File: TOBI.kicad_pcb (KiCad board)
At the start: 4 copper layers, 50.8 x 50.8 mm, 23 parts, among them J1 Battery Connector, J2 Top Screw Terminal, J3 Bottom Screw Terminal, Q1 Q_NMOS_GDS, Q2 Q_NMOS_GDS, Q3 Q_NMOS_GDS, U1 XIAO-ESP32-S3-SMD, U2 LSM6DSO32, U4 MS5611-01BA

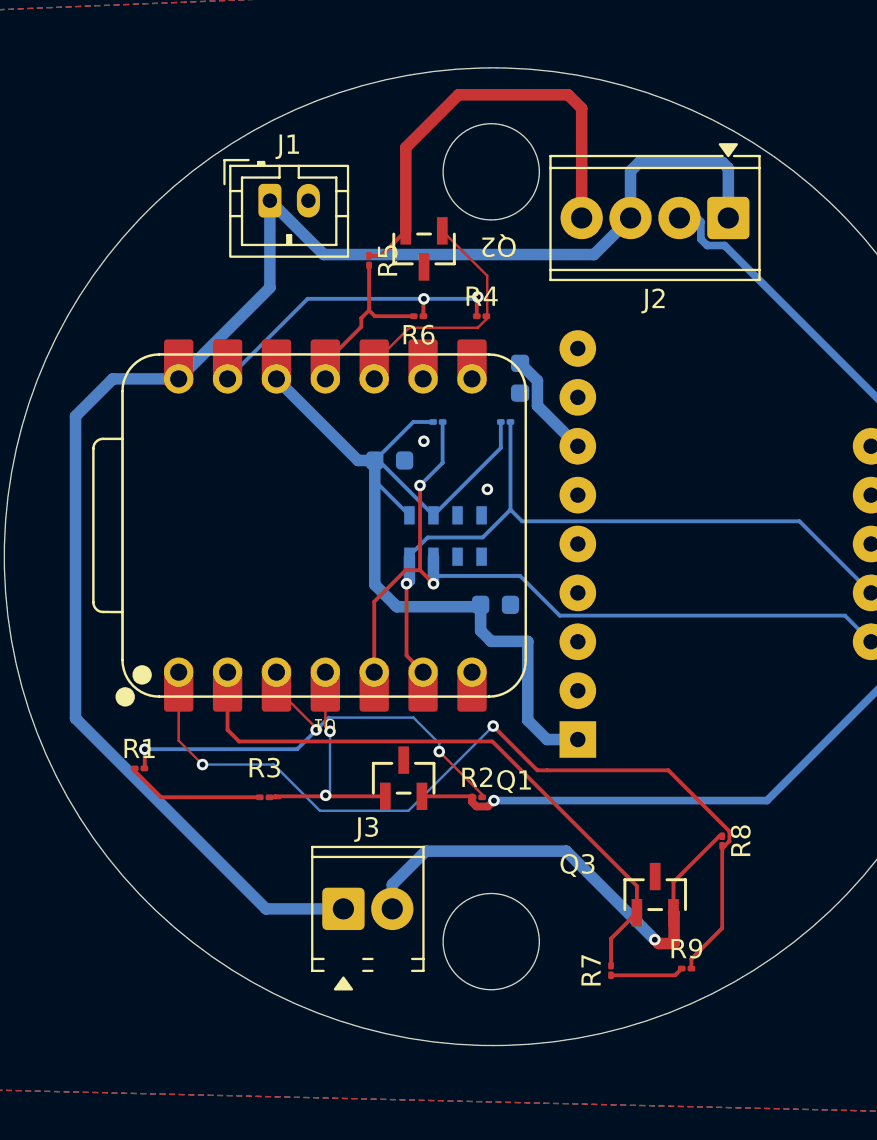
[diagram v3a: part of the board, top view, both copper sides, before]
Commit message: Silkscreen Text Modifications
Added more descriptive text, edited sizes for labeling, as well as general board info text.
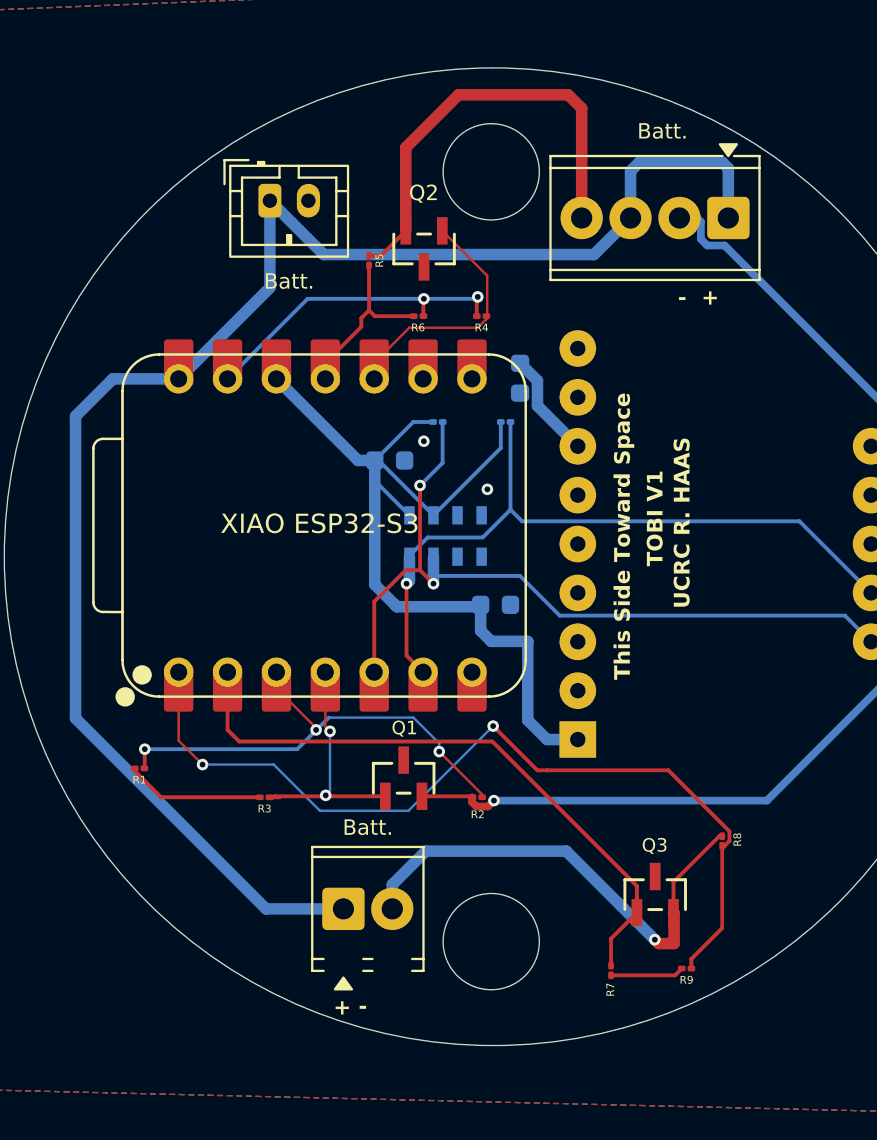
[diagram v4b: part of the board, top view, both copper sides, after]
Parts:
- XIAO ESP32-S3: renamed from U1
- renumbered J3 to Batt., J2 to Batt., J1 to Batt., U4 to IMU, U2 to LSM6DSO32
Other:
- board text added: "+ -"
- board text added: "- +"
- board text added: "TOBI V1"
- board text added: "This Side Toward Space"
- board text added: "UCRC R. HAAS"
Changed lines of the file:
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@@
 		(tags "resistor")
 		(property "Reference" "R5"
-			(at 0 -1 90)
+			(at 0 -0.549199 90)
 			(layer "F.SilkS")
 			(effects
 				(font
-					(size 1 1)
-					(thickness 0.15)
+					(size 0.4 0.4)
+					(thickness 0.05)
 				)
 			)
@@
 		(tags "T2N7002BK_LM ")
 		(property "Reference" "Q1"
-			(at 5.760001 0.1298 0)
+			(at 0.049999 -2.610201 0)
 			(unlocked yes)
 			(layer "F.SilkS")
 			(effects
 				(font
-					(size 1 1)
-					(thickness 0.15)
+					(size 0.7 0.7)
+					(thickness 0.0875)
 				)
 			)
@@
 		(tags "resistor")
 		(property "Reference" "R3"
-			(at 0 -1.5 0)
+			(at 0 0.6 0)
 			(layer "F.SilkS")
 			(effects
 				(font
-					(size 1 1)
-					(thickness 0.15)
+					(size 0.4 0.4)
+					(thickness 0.05)
 				)
 			)
@@
 		(layer "F.Cu")
 		(at 183.88 100.88 180)
-		(property "Reference" "U1"
-			(at 0.025 -10.35 180)
+		(property "Reference" "XIAO ESP32-S3"
+			(at 0.28 0.08 0)
 			(unlocked yes)
 			(layer "F.SilkS")
 			(effects
 				(font
-					(size 0.635 0.635)
-					(thickness 0.1016)
+					(size 1 1)
+					(thickness 0.125)
 				)
 			)
@@
 		(descr "Terminal Block Phoenix MPT-0,5-2-2.54, 2 pins, pitch 2.54mm, size 5.54x6.2mm, drill diameter 1.1mm, pad diameter 2.2mm, http://www.mouser.com/ds/2/324/ItemDetail_1725656-920552.pdf, script-generated using https://gitlab.com/kicad/libraries/kicad-footprint-generator/-/tree/master/scripts/TerminalBlock_Phoenix")
 		(tags "THT Terminal Block Phoenix MPT-0,5-2-2.54 pitch 2.54mm size 5.54x6.2mm drill 1.1mm pad 2.2mm")
-		(property "Reference" "J3"
+		(property "Reference" "Batt."
 			(at 1.27 -4.22 0)
 			(layer "F.SilkS")
 			(effects
 				(font
-					(size 1 1)
-					(thickness 0.15)
+					(size 0.8 0.8)
+					(thickness 0.1)
 				)
 			)
@@
 		(tags "resistor")
 		(property "Reference" "R1"
-			(at 0 -1 0)
+			(at 0 0.6 0)
 			(layer "F.SilkS")
 			(effects
 				(font
-					(size 1 1)
-					(thickness 0.15)
+					(size 0.4 0.4)
+					(thickness 0.05)
 				)
 			)
@@
 		(tags "resistor")
 		(property "Reference" "R9"
-			(at 0 -1 0)
+			(at 0 0.6 0)
 			(layer "F.SilkS")
 			(effects
 				(font
-					(size 1 1)
-					(thickness 0.15)
+					(size 0.4 0.4)
+					(thickness 0.05)
 				)
 			)
@@
 		(tags "resistor")
 		(property "Reference" "R2"
-			(at 0 -1 0)
+			(at 0.025 0.9 0)
 			(layer "F.SilkS")
 			(effects
 				(font
-					(size 1 1)
-					(thickness 0.15)
+					(size 0.4 0.4)
+					(thickness 0.05)
 				)
 			)
@@
 		(descr "Terminal Block Phoenix MPT-0,5-4-2.54, 4 pins, pitch 2.54mm, size 10.6x6.2mm, drill diameter 1.1mm, pad diameter 2.2mm, http://www.mouser.com/ds/2/324/ItemDetail_1725672-916605.pdf, script-generated using https://gitlab.com/kicad/libraries/kicad-footprint-generator/-/tree/master/scripts/TerminalBlock_Phoenix")
 		(tags "THT Terminal Block Phoenix MPT-0,5-4-2.54 pitch 2.54mm size 10.6x6.2mm drill 1.1mm pad 2.2mm")
-		(property "Reference" "J2"
-			(at 3.81 -4.22 0)
+		(property "Reference" "Batt."
+			(at 3.42 4.5 0)
 			(layer "F.SilkS")
 			(effects
 				(font
-					(size 1 1)
-					(thickness 0.15)
+					(size 0.8 0.8)
+					(thickness 0.1)
 				)
 			)
@@
 		(tags "T2N7002BK_LM ")
 		(property "Reference" "Q2"
-			(at -3.864999 0.1298 180)
+			(at 0.0108 2.908599 0)
 			(unlocked yes)
 			(layer "F.SilkS")
 			(effects
 				(font
-					(size 1 1)
-					(thickness 0.15)
+					(size 0.8 0.8)
+					(thickness 0.1)
 				)
 			)
@@
 		(tags "resistor")
 		(property "Reference" "R6"
-			(at 0 -1 0)
+			(at 0.025 -0.6 0)
 			(layer "F.SilkS")
 			(effects
 				(font
-					(size 1 1)
-					(thickness 0.15)
+					(size 0.4 0.4)
+					(thickness 0.05)
 				)
 			)
@@
 		(tags "T2N7002BK_LM ")
 		(property "Reference" "Q3"
-			(at -4.019999 -1.5602 0)
+			(at -0.019999 -2.5602 0)
 			(unlocked yes)
 			(layer "F.SilkS")
 			(effects
 				(font
-					(size 1 1)
-					(thickness 0.15)
+					(size 0.7 0.7)
+					(thickness 0.0875)
 				)
 			)
@@
 		(descr "JST PH series connector, B2B-PH-K (http://www.jst-mfg.com/product/pdf/eng/ePH.pdf), generated with kicad-footprint-generator")
 		(tags "connector JST PH vertical")
-		(property "Reference" "J1"
-			(at 1 -2.9 0)
+		(property "Reference" "Batt."
+			(at 1 4.2 0)
 			(layer "F.SilkS")
 			(effects
 				(font
-					(size 1 1)
-					(thickness 0.15)
+					(size 0.8 0.8)
+					(thickness 0.1)
 				)
 			)
@@
 		(tags "resistor")
 		(property "Reference" "R4"
-			(at 0 -1 0)
+			(at 0 0.6 0)
 			(layer "F.SilkS")
 			(effects
 				(font
-					(size 1 1)
-					(thickness 0.15)
+					(size 0.4 0.4)
+					(thickness 0.05)
 				)
 			)
@@
 		(tags "resistor")
 		(property "Reference" "R7"
-			(at 0 -1 90)
+			(at -1 -0.025 270)
 			(layer "F.SilkS")
 			(effects
 				(font
-					(size 1 1)
-					(thickness 0.15)
+					(size 0.4 0.4)
+					(thickness 0.05)
 				)
 			)
@@
 		(tags "resistor")
 		(property "Reference" "R8"
-			(at 0 -1 90)
+			(at -0.075 -0.8 90)
 			(layer "F.SilkS")
 			(effects
 				(font
-					(size 1 1)
-					(thickness 0.15)
+					(size 0.4 0.4)
+					(thickness 0.05)
 				)
 			)
@@
 			(effects
 				(font
-					(size 1 1)
-					(thickness 0.15)
+					(size 0.4 0.4)
+					(thickness 0.05)
 				)
 				(justify mirror)
@@
 		(tags "resistor")
 		(property "Reference" "R11"
-			(at 0 1 0)
+			(at 0 0.7 0)
 			(layer "B.SilkS")
 			(effects
 				(font
-					(size 1 1)
-					(thickness 0.15)
+					(size 0.4 0.4)
+					(thickness 0.05)
 				)
 				(justify mirror)
@@
 		(tags "capacitor")
 		(property "Reference" "C4"
-			(at 0 1.43 90)
+			(at 2.425 0.1 90)
 			(layer "B.SilkS")
 			(effects
 				(font
-					(size 1 1)
-					(thickness 0.15)
+					(size 0.8 0.8)
+					(thickness 0.1)
 				)
 				(justify mirror)
@@
 		(tags "capacitor")
 		(property "Reference" "C3"
-			(at -3.665 0.19 0)
+			(at 0.025 1.7 0)
 			(layer "B.SilkS")
 			(effects
 				(font
-					(size 1 1)
-					(thickness 0.15)
+					(size 0.8 0.8)
+					(thickness 0.1)
 				)
 				(justify mirror)
@@
 		(tags "capacitor")
 		(property "Reference" "C5"
-			(at 0 2.145 0)
+			(at -0.075 -1.5 0)
 			(layer "B.SilkS")
 			(effects
 				(font
-					(size 1 1)
-					(thickness 0.15)
+					(size 0.8 0.8)
+					(thickness 0.1)
 				)
 				(justify mirror)
@@
 		(layer "B.Cu")
 		(at 204.62 101.84 90)
-		(property "Reference" "U2"
-			(at -5.08 -1.27 270)
+		(property "Reference" "LSM6DSO32"
+			(at 8.04 0.78 0)
 			(unlocked yes)
 			(layer "B.SilkS")
@@
 		)
 		(fp_text user "DOG"
-			(at 3.25 3.5 180)
+			(at 2.04 6.58 0)
 			(unlocked yes)
 			(layer "B.SilkS")
@@
 		)
 		(fp_text user "SDX"
-			(at -2 3.5 180)
+			(at -2.96 6.48 0)
 			(unlocked yes)
 			(layer "B.SilkS")
@@
 		)
 		(fp_text user "SCX"
-			(at -4.5 3.5 180)
+			(at -5.66 6.58 0)
 			(unlocked yes)
 			(layer "B.SilkS")
@@
 		)
 		(fp_text user "CS"
-			(at 0.75 4.5 180)
+			(at -0.66 6.58 0)
 			(unlocked yes)
 			(layer "B.SilkS")
@@
 		)
 		(fp_text user "ND"
-			(at 5.75 4.5 180)
+			(at 4.54 6.48 0)
 			(unlocked yes)
 			(layer "B.SilkS")
@@
 		(descr "LGA-8")
 		(tags "lga land grid array")
-		(property "Reference" "U4"
-			(at -0.715 3.65 90)
+		(property "Reference" "IMU"
+			(at -2.525 0.025 180)
 			(layer "B.SilkS")
 			(effects
 				(font
-					(size 1 1)
-					(thickness 0.15)
+					(size 0.8 0.8)
+					(thickness 0.1)
 				)
 				(justify mirror)
@@
 		(layer "Edge.Cuts")
 	)
+	(gr_text "-  +"
+		(at 202.2 89.5 0)
+		(layer "F.SilkS")
+		(effects
+			(font
+				(size 0.8 0.8)
+				(thickness 0.16)
+				(bold yes)
+			)
+			(justify left bottom)
+		)
+	)
+	(gr_text "+ -"
+		(at 184.3 125.5 180)
+		(layer "F.SilkS")
+		(effects
+			(font
+				(size 0.8 0.8)
+				(thickness 0.16)
+				(bold yes)
+			)
+			(justify left bottom mirror)
+		)
+	)
+	(gr_text "This Side Toward Space"
+		(at 199.8 108.9 90)
+		(layer "F.SilkS")
+		(effects
+			(font
+				(size 0.8128 0.8128)
+				(thickness 0.1524)
+				(bold yes)
+			)
+			(justify left bottom)
+		)
+	)
+	(gr_text "TOBI V1"
+		(at 201.5 103 90)
+		(layer "F.SilkS")
+		(effects
+			(font
+				(size 0.8128 0.8128)
+				(thickness 0.1524)
+				(bold yes)
+			)
+			(justify left bottom)
+		)
+	)
+	(gr_text "UCRC R. HAAS"
+		(at 202.9 105.2 90)
+		(layer "F.SilkS")
+		(effects
+			(font
+				(size 0.8128 0.8128)
+				(thickness 0.1524)
+				(bold yes)
+			)
+			(justify left bottom)
+		)
+	)
 	(segment

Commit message: Final PCB
Final PCB that is being pushed out, DRC checks fine
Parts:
- U1: renamed from XIAO ESP32-S3
- renumbered Batt. to J1, Batt. to J2, Batt. to J3, LSM6DSO32 to U2, IMU to U4
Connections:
- C3 pad 1: GND -> -BATT
- C4 pad 1: GND -> -BATT
- C5 pad 1: GND -> -BATT
- Q1 pad 3: GND -> -BATT
- Q2 pad 3: GND -> -BATT
- Q3 pad 3: GND -> -BATT
- R1 pad 1: GND -> -BATT
- R3 pad 1: GND -> -BATT
- R4 pad 1: GND -> -BATT
- R6 pad 1: GND -> -BATT
- R7 pad 1: GND -> -BATT
- R9 pad 1: GND -> -BATT
- U1 pad 13: GND -> -BATT
- U2 pad 12: GND -> -BATT
- U2 pad 3: GND -> -BATT
- U2 pad 4: GND -> -BATT
- U2 pad 5: GND -> -BATT
- U4 pad 3: GND -> -BATT
- U4 pad 4: GND -> -BATT
- U4 pad 5: GND -> -BATT
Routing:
- net -BATT: track 0.00 -> 27.8 mm, vias 0 -> 5
- net GND: track 27.7 -> 0.00 mm, vias 4 -> 0
- added copper zone on B.Cu, net -BATT
- added copper zone on F.Cu, net -BATT
- removed copper zone on B.Cu, net GND
- removed copper zone on F.Cu, net GND
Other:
- rule solder_mask_min_width: 0.12 -> 0.1

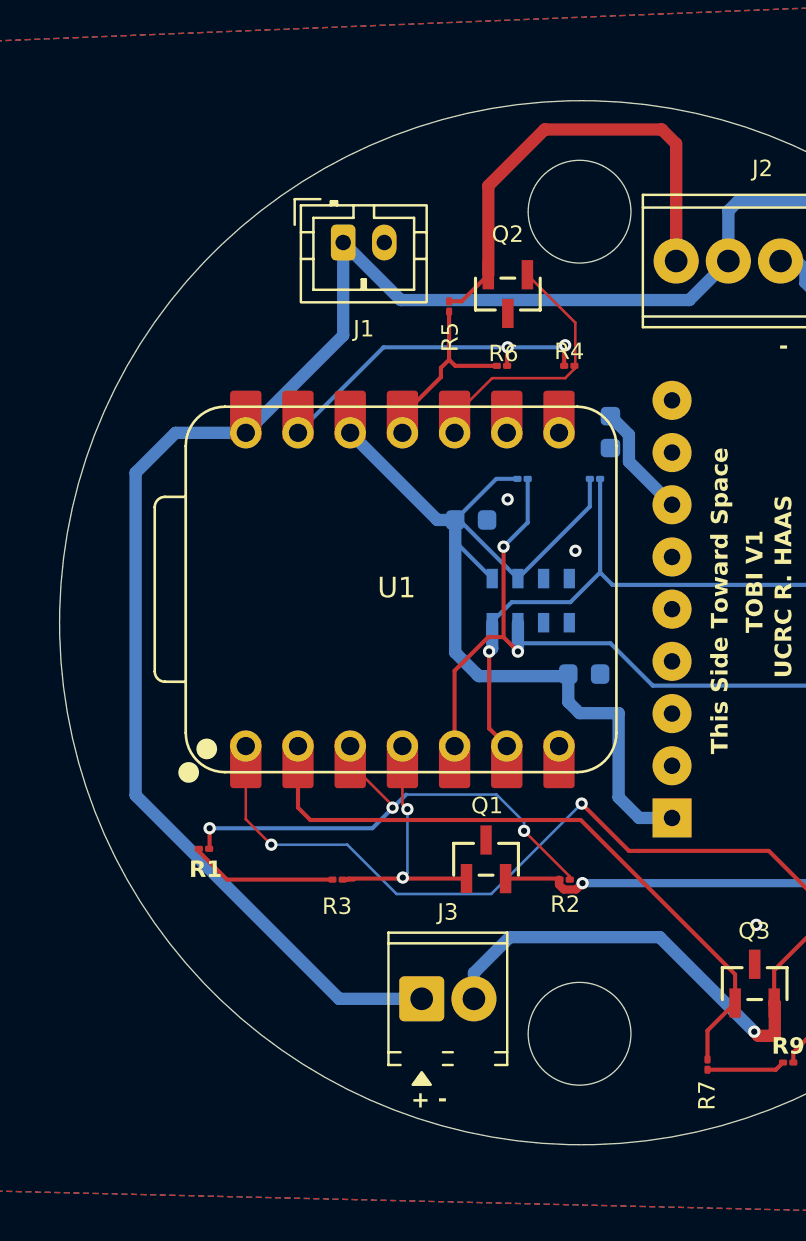
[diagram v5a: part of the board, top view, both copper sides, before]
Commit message: Additional Final Changes for Gerber
Little tweaks for threaded rod holes, version pushed to JLC PBC.
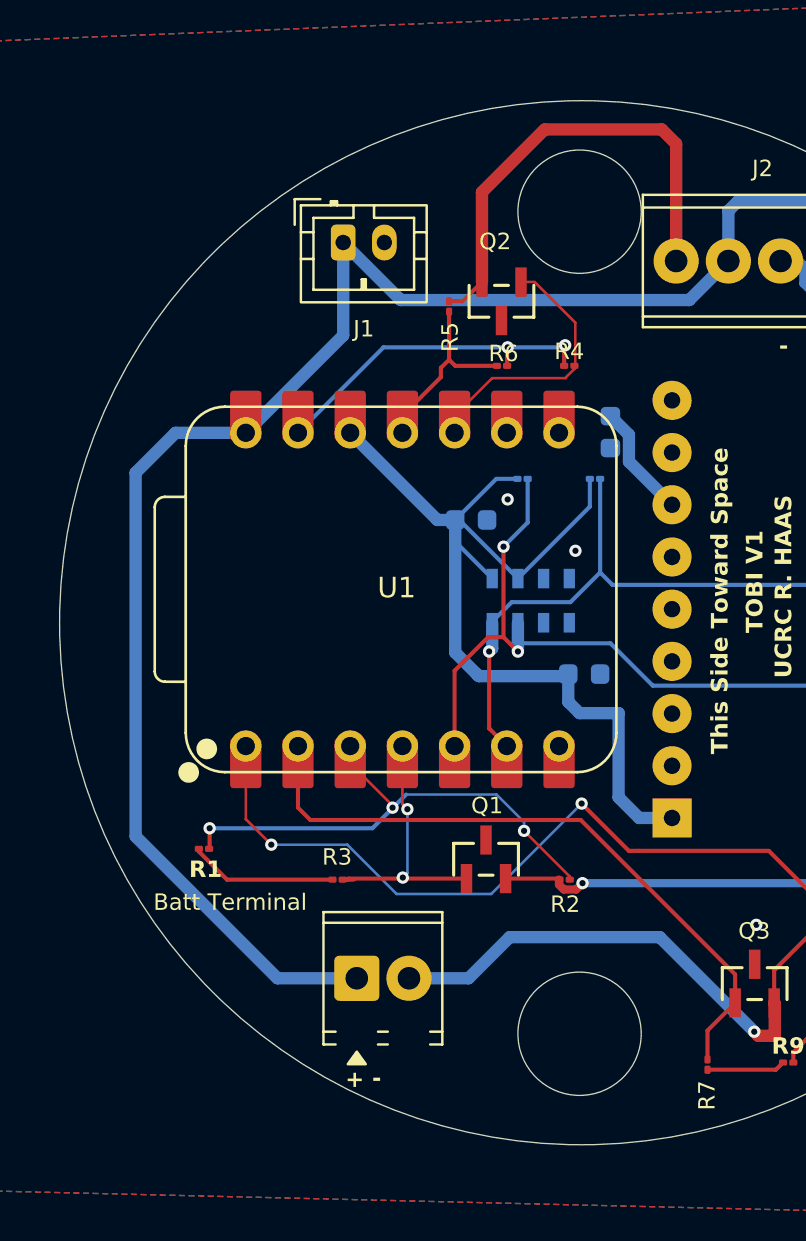
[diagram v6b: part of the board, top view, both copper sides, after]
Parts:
- added REF**: MountingHole_6mm, MountingHole:MountingHole_6mm, F.Cu at (192.5, 82.5)
- added REF**: MountingHole_6mm, MountingHole:MountingHole_6mm, F.Cu at (192.5, 122.5)
- Batt Terminal: renamed from J3
- moved Batt Terminal 3.31 mm to (181.7, 119.8)
- moved Q2 0.47 mm to (188.7, 86.9)
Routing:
- net +BATT: track 82.2 -> 79.8 mm
- net /MOTOR: track 25.3 -> 27.3 mm
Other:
- outline, holes or cut-outs redrawn
